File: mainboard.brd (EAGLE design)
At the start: 104.8 x 57.1 mm, 16 parts, among them IC1 7805TV, IC2 7805TV, IC3 7805TV, X1 22-23-2021

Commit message: Add files via upload
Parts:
- removed PERIFERAL: (no value), con-lstb:MA04-1
- removed R3: 120, rcl:0204/7
- removed U$2: PIN_2X2, DUElib130425:PIN_2X2
- removed V4: ALTIMETER_V4, aero_sensors:ALTIMETER_V4
- added MUX1, MUX2: SN74HC157, QADT:SN74HC157
- added R1: 100k, rcl:0204/7
- added U$4: ALTIMETER_V5, aero_sensors:ALTIMETER_V5
- G1: device aero_sensors:GPS_ADAFRUIT -> QADT:GPS_ADAFRUIT
- OUT: value PIN_3X8 -> PIN_3X9; device aero_sensors:PIN_3X8 -> QADT:PIN_3X9
- R2: value 120 -> 30k
- moved MPU 21.2 mm to (65.8, 23.0), turned to 90 degrees
- moved R2 13.1 mm to (68.1, 16.1), turned to 180 degrees
- moved X1 6.05 mm to (24.3, 6.35)
- moved IC3 4.58 mm to (46.5, 15.2)
- moved IC2 3.57 mm to (38.6, 15.2)
- moved G1 3.45 mm to (46.0, 38.4)
- moved XB1 2.99 mm to (82.2, 38.5)
- moved OUT 1.91 mm to (13.1, 17.7)
- moved U$1 1.80 mm to (78.2, 23.1)
- moved U$3 1.80 mm to (8.13, 5.08)
- moved IC1 1.80 mm to (30.2, 15.2)
- moved REC 1.27 mm to (14.0, 49.0)
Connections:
- removed net FLAP_MODE: REC.3.5, U$1.11
- removed net LED_ON: PERIFERAL.4, R3.1
- removed net LED_TEST: R2.2, U$1.50
- removed net LED_TEST_OUT: PERIFERAL.3, R2.1
- removed net LEFT_TAIL: OUT.3.7, U$1.3
- removed net N$1: U$1.GND_1
- removed net N$3: U$2.1.1, XB1.3
- removed net N$4: U$2.1.2, XB1.2
- removed net PID_MODE: REC.3.6, U$1.7
- removed net PITCH_R: REC.3.3, U$1.8
- removed net RIGHT_TAIL: OUT.3.5, U$1.4
- removed net ROLL_R: REC.3.2, U$1.9
- removed net RUDDER: OUT.3.8, U$1.2
- removed net RX1: G1.RX, U$1.RX1
- removed net SPARE: OUT.3.1, U$1.13
- removed net TX1: G1.TX, U$1.TX1
- removed net YAW_R: REC.3.4, U$1.12
- new net BATTERY_VOLTAGE_IN: R1.1, R2.2, U$1.A4
- new net DUE-TO-GPS: G1.RX, U$1.TX1
- new net FLAPS_IN: MUX2.11, MUX2.14, REC.3.6, U$1.50
- new net FLAPS_LEFT: MUX2.12, OUT.3.8
- new net FLAPS_LEFT_AOUT: MUX2.13, U$1.7
- new net FLAPS_RIGHT: MUX2.9, OUT.3.9
- new net FLAPS_RIGHT_AOUT: MUX2.10, U$1.8
- new net GPS-TO-DUE: G1.TX, U$1.RX1
- new net LEFT_AILERON_AOUT: MUX1.3, U$1.5
- new net LEFT_AILERON_IN: MUX1.2, REC.3.2, U$1.9
- new net LEFT_VTAIL: MUX2.4, OUT.3.4
- new net LEFT_VTAIL_AOUT: MUX2.3, U$1.3
- new net LEFT_VTAIL_IN: MUX2.2, REC.3.4, U$1.11
- new net RIGHT_AILERON_AOUT: MUX1.6, U$1.6
- new net RIGHT_AILERON_IN: MUX1.5, REC.3.3, U$1.10
- new net RIGHT_VTAIL: MUX2.7, OUT.3.5
- new net RIGHT_VTAIL_AOUT: MUX2.6, U$1.4
- new net RIGHT_VTAIL_IN: MUX2.5, REC.3.5, U$1.12
- new net TAIL_WHEEL: OUT.3.7, U$1.2
- net +5V: now also MUX1.1, MUX2.1; no longer REC.2.1, REC.2.2, REC.2.3, REC.2.4, REC.2.5, REC.2.6, V4.VIN
- net 12V: now also R1.2
- net 3.3V: now also U$4.VIN; no longer R3.2
- net DROP: now also OUT.3.1, U$1.13; no longer OUT.3.2, U$1.10
- net GND: now also MUX1.15, MUX1.8, MUX2.15, MUX2.8, OUT.1.9, R2.1, U$1.GND_1, U$4.GND; no longer PERIFERAL.1, V4.GND
- net LEFT_AILERON: now also MUX1.4, OUT.3.2; no longer OUT.3.3, U$1.6
- net RESET: no longer PERIFERAL.2
- net RIGHT_AILERON: now also MUX1.7, OUT.3.3; no longer OUT.3.4, U$1.5
- net RX: now also XB1.2; no longer U$2.2.2
- net SCL: now also U$4.SCL; no longer V4.SCL
- net SDA: now also U$4.SDA; no longer V4.SDA
- net SERVO_PWR: now also MUX1.16, MUX2.16, OUT.2.9, REC.2.1, REC.2.2, REC.2.3, REC.2.4, REC.2.5, REC.2.6
- net TX: now also XB1.3; no longer U$2.2.1
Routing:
- net FLAPS_IN: track 0.00 -> 190.6 mm, vias 0 -> 5
- net SERVO_PWR: track 46.6 -> 190.3 mm, vias 0 -> 3
- net LEFT_VTAIL_IN: track 0.00 -> 111.8 mm, vias 0 -> 5
- net +5V: track 154.7 -> 71.1 mm, vias 2 -> 1
- net TX1: track 75.4 -> 0.00 mm, vias 2 -> 0
- net RIGHT_TAIL: track 70.7 -> 0.00 mm
- net LEFT_TAIL: track 69.1 -> 0.00 mm
- net RUDDER: track 69.1 -> 0.00 mm
- net TAIL_WHEEL: track 0.00 -> 68.6 mm
- net RESET: track 65.3 -> 0.00 mm, vias 2 -> 0
- net LEFT_AILERON_IN: track 0.00 -> 63.8 mm, vias 0 -> 1
- net PID_MODE: track 61.7 -> 0.00 mm
- net FLAP_MODE: track 59.9 -> 0.00 mm
- net RIGHT_AILERON_IN: track 0.00 -> 58.3 mm, vias 0 -> 2
- net SPARE: track 57.7 -> 0.00 mm, vias 1 -> 0
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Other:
- board size 104.8 x 57.1 mm -> 103.5 x 57.2 mm
- board text added: "FL"
- board text added: "GND"
- board text added: "LF"
- board text added: "RF"
- board text added: "TW"
- board text removed: "ELV"
- board text removed: "G"
- board text removed: "P"
- board text removed: "PID"
- board text removed: "PROG"
- board text removed: "R"
- board text removed: "RU"
- board text removed: "SP"
- board text removed: "T"

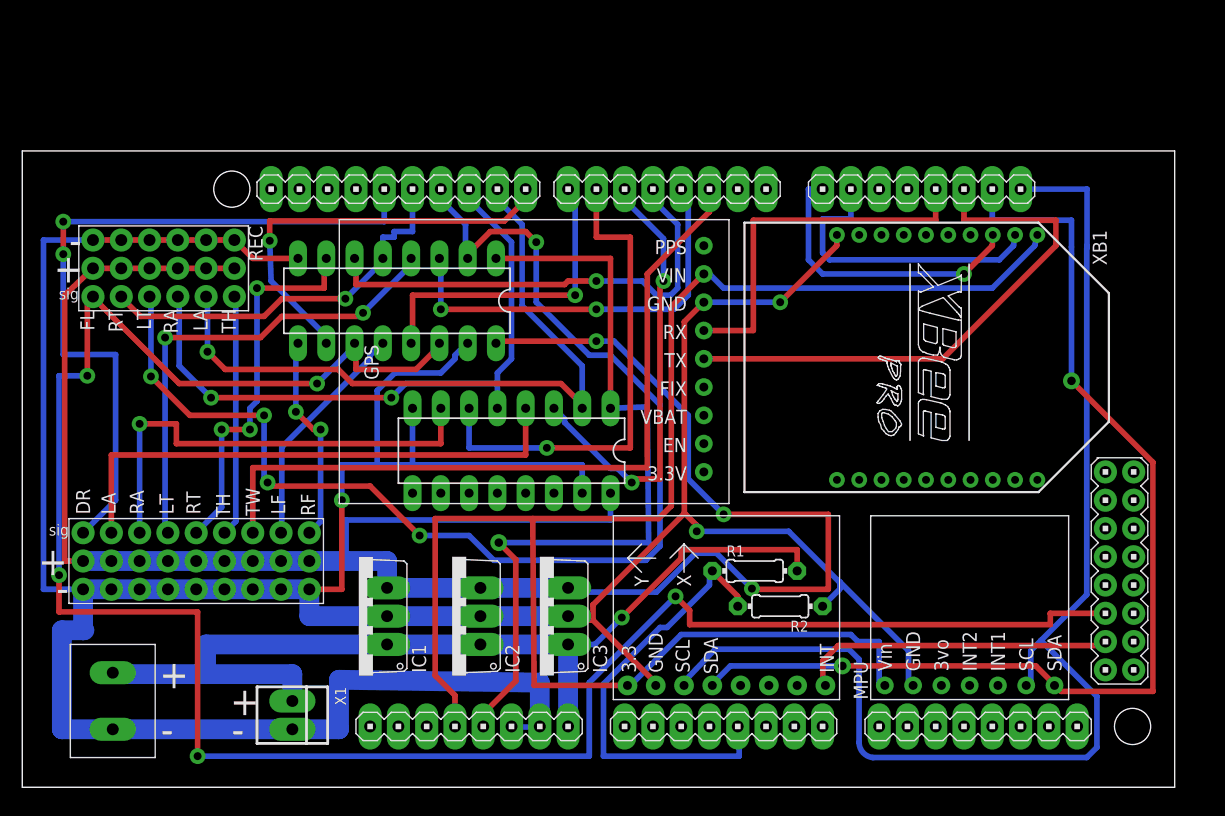
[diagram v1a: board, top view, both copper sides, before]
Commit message: Board with Four Holes
Added top-right and bottom-left hole
Hole placement based on Arduino due eagle file found on Arduino.com
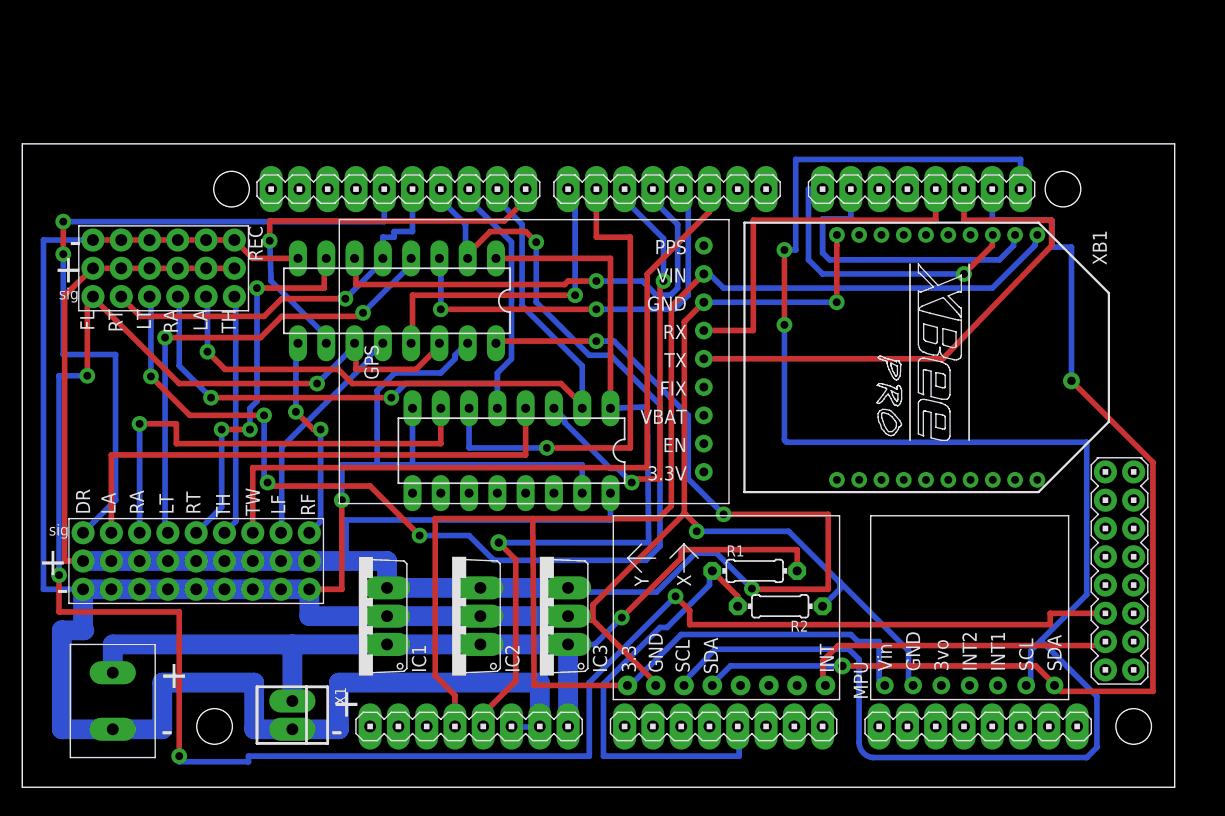
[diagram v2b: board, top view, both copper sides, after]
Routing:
- net SCL: track 111.9 -> 159.5 mm, vias 0 -> 2
- net GND: track 323.4 -> 334.5 mm
- net 12V: track 88.2 -> 83.0 mm
- net FLAPS_IN: track 190.6 -> 191.6 mm
- net GPS-TO-DUE: track 49.2 -> 48.5 mm
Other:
- board size 103.5 x 57.2 mm -> 103.5 x 57.8 mm

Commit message: Add files via upload
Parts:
- OUT: value PIN_3X9 -> PIN_3X10; device QADT:PIN_3X9 -> QADT:PIN_3X10
- moved MUX1 16.6 mm to (34.2, 43.6), turned to 0 degrees
- moved MUX2 16.4 mm to (43.1, 30.1), turned to 0 degrees
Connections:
- new net MUX_SELECT_A: MUX1.1, U$1.44
- new net MUX_SELECT_B: MUX2.1, U$1.46
- new net SPARE: OUT.3.10, U$1.9
- net +5V: no longer MUX1.1, MUX2.1
- net GND: now also OUT.1.10; no longer MUX1.15
- net LEFT_AILERON_IN: now also U$1.40; no longer U$1.9
- net LEFT_VTAIL: now also MUX1.12; no longer MUX2.4
- net LEFT_VTAIL_AOUT: now also MUX1.13; no longer MUX2.3
- net LEFT_VTAIL_IN: now also MUX1.14, MUX1.15; no longer MUX2.2
- net RIGHT_VTAIL: now also MUX1.9; no longer MUX2.7
- net RIGHT_VTAIL_AOUT: now also MUX1.10; no longer MUX2.6
- net RIGHT_VTAIL_IN: now also MUX1.11; no longer MUX2.5
- net SERVO_PWR: now also OUT.2.10
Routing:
- net LEFT_AILERON_IN: track 63.8 -> 188.5 mm, vias 1 -> 5
- net LEFT_VTAIL: track 43.1 -> 147.3 mm, vias 2 -> 3
- net MUX_SELECT_B: track 0.00 -> 102.3 mm, vias 0 -> 6
- net MUX_SELECT_A: track 0.00 -> 90.5 mm, vias 0 -> 6
- net LEFT_VTAIL_IN: track 111.8 -> 33.8 mm, vias 5 -> 0
- net SPARE: track 0.00 -> 74.8 mm, vias 0 -> 3
- net +5V: track 71.1 -> 0.00 mm, vias 1 -> 0
- net GND: track 334.5 -> 302.0 mm
- net FLAPS_RIGHT: track 18.8 -> 50.8 mm, vias 2 -> 1
- net FLAPS_LEFT: track 20.8 -> 50.0 mm, vias 0 -> 1
- net RIGHT_VTAIL_AOUT: track 42.0 -> 19.4 mm
- net 3.3V: track 148.4 -> 131.0 mm
- net SERVO_PWR: track 190.3 -> 173.6 mm
- net FLAPS_RIGHT_AOUT: track 37.8 -> 25.1 mm
- net RIGHT_AILERON_AOUT: track 44.3 -> 32.9 mm, vias 1 -> 2
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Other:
- board size 103.5 x 57.8 mm -> 104.6 x 57.8 mm
- board text added: "SP"

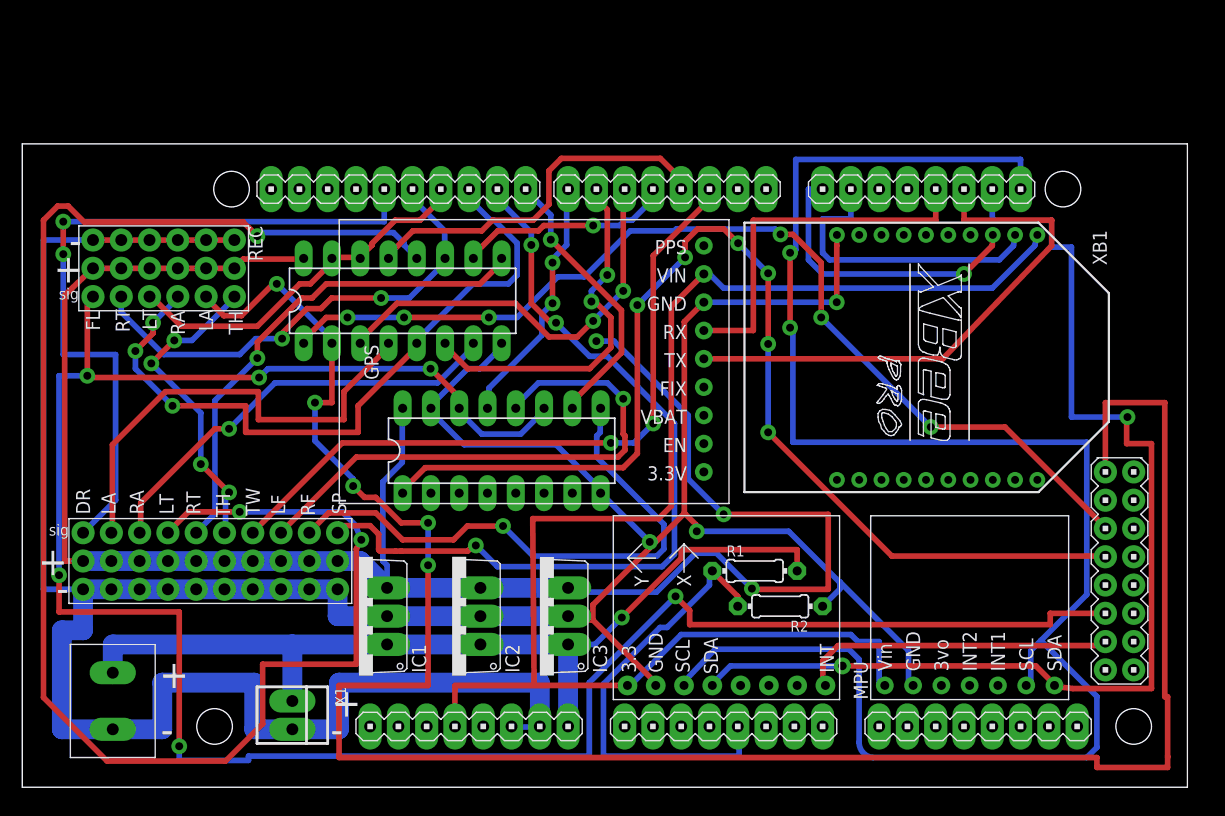
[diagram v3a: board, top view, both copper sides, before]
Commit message: ERC error fixed
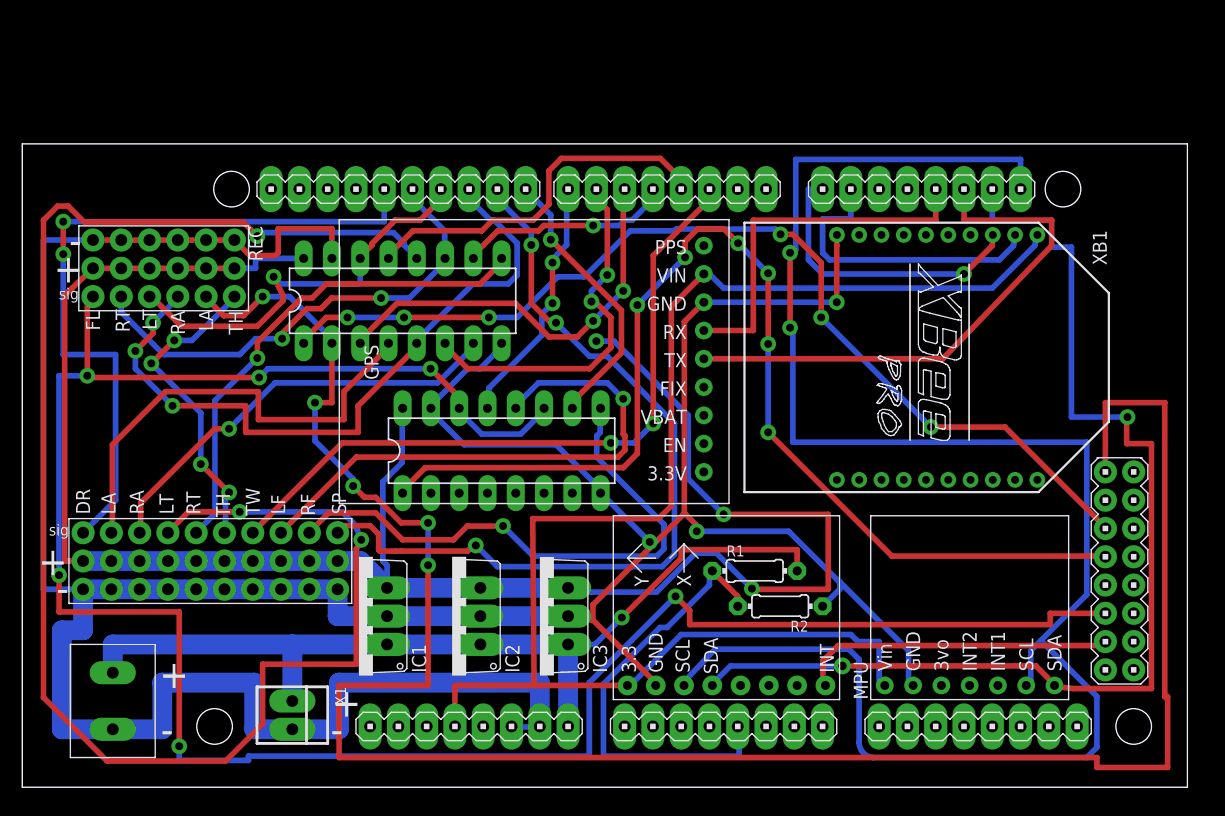
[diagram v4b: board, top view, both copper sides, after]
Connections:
- net GND: now also MUX1.15
- net LEFT_VTAIL_IN: no longer MUX1.15
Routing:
- net GND: track 302.0 -> 316.3 mm
- net LEFT_VTAIL_IN: track 33.8 -> 37.4 mm, vias 0 -> 1
- net LEFT_AILERON_IN: track 188.5 -> 187.6 mm
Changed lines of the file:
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@@
 <wire x1="52.07" y1="26.19375" x2="51.943" y2="26.289" width="0.508" layer="16"/>
 <via x="56.35625" y="21.9075" extent="1-16" drill="0.7112"/>
+<contactref element="MUX1" pad="15"/>
+<wire x1="19.05" y1="49.022" x2="20.447" y2="47.625" width="0.508" layer="1"/>
+<wire x1="20.447" y1="47.625" x2="22.733" y2="47.625" width="0.508" layer="1"/>
+<wire x1="22.733" y1="47.625" x2="22.987" y2="47.879" width="0.508" layer="1"/>
+<wire x1="22.987" y1="47.879" x2="22.987" y2="50.038" width="0.508" layer="1"/>
+<wire x1="22.987" y1="50.038" x2="27.813" y2="50.038" width="0.508" layer="1"/>
+<wire x1="27.813" y1="50.038" x2="27.813" y2="47.371" width="0.508" layer="1"/>
 </signal>
 <signal name="LEFT_AILERON">
@@
 <wire x1="32.385" y1="20.193" x2="32.385" y2="27.305" width="0.508" layer="16"/>
 <wire x1="34.13125" y1="33.81375" x2="34.163" y2="33.909" width="0.508" layer="16"/>
-<wire x1="19.84375" y1="47.3075" x2="25.24125" y2="47.3075" width="0.508" layer="1"/>
-<wire x1="19.20875" y1="46.6725" x2="19.84375" y2="47.3075" width="0.508" layer="1"/>
-<wire x1="25.24125" y1="47.3075" x2="25.273" y2="47.371" width="0.508" layer="1"/>
-<wire x1="19.20875" y1="46.6725" x2="19.05" y2="46.482" width="0.508" layer="1"/>
 <wire x1="32.766" y1="17.78" x2="30.353" y2="20.193" width="1.778" layer="16"/>
 <wire x1="30.353" y1="20.193" x2="28.321" y2="20.193" width="1.778" layer="16"/>
 <wire x1="32.385" y1="20.193" x2="32.766" y2="19.812" width="0.508" layer="16"/>
 <wire x1="32.766" y1="19.812" x2="32.766" y2="17.78" width="0.508" layer="16"/>
+<wire x1="25.273" y1="47.371" x2="20.955" y2="47.371" width="0.508" layer="16"/>
+<wire x1="20.955" y1="47.371" x2="20.955" y2="46.482" width="0.508" layer="16"/>
+<wire x1="20.955" y1="46.482" x2="19.05" y2="46.482" width="0.508" layer="16"/>
 </signal>
 <signal name="12V">
@@
 <contactref element="MUX1" pad="2"/>
 <wire x1="27.78125" y1="40.16375" x2="27.78125" y2="39.84625" width="0.508" layer="16"/>
-<wire x1="22.86" y1="45.085" x2="27.78125" y2="40.16375" width="0.508" layer="16"/>
-<wire x1="22.5425" y1="45.085" x2="22.86" y2="45.085" width="0.508" layer="1"/>
-<wire x1="19.685" y1="42.2275" x2="22.5425" y2="45.085" width="0.508" layer="1"/>
-<wire x1="18.0975" y1="42.2275" x2="19.685" y2="42.2275" width="0.508" layer="1"/>
+<wire x1="18.0975" y1="42.2275" x2="19.8755" y2="42.2275" width="0.508" layer="1"/>
 <wire x1="16.51" y1="43.815" x2="18.0975" y2="42.2275" width="0.508" layer="1"/>
 <wire x1="27.78125" y1="39.84625" x2="27.813" y2="39.751" width="0.508" layer="16"/>
 <wire x1="16.51" y1="43.815" x2="16.51" y2="43.942" width="0.508" layer="1"/>
-<via x="22.86" y="45.085" extent="1-16" drill="0.7112"/>
+<via x="21.59" y="43.942" extent="1-16" drill="0.7112"/>
 <contactref element="U$1" pad="40"/>
 <wire x1="97.282" y1="28.194" x2="97.282" y2="34.417" width="0.508" layer="1"/>
@@
 <wire x1="102.616" y1="34.417" x2="102.616" y2="8.001" width="0.508" layer="1"/>
 <wire x1="102.616" y1="8.001" x2="102.87" y2="8.001" width="0.508" layer="1"/>
-<wire x1="102.87" y1="8.001" x2="102.87" y2="2.667" width="0.508" layer="1"/>
-<wire x1="102.87" y1="2.667" x2="102.87" y2="2.54" width="0.508" layer="1"/>
+<wire x1="102.87" y1="8.001" x2="102.87" y2="1.651" width="0.508" layer="1"/>
 <wire x1="28.448" y1="2.54" x2="96.52" y2="2.54" width="0.508" layer="1"/>
 <wire x1="96.52" y1="2.54" x2="96.52" y2="1.651" width="0.508" layer="1"/>
 <wire x1="96.52" y1="1.651" x2="102.87" y2="1.651" width="0.508" layer="1"/>
-<wire x1="102.87" y1="1.651" x2="102.87" y2="2.54" width="0.508" layer="1"/>
+<wire x1="27.78125" y1="40.16375" x2="24.003" y2="43.942" width="0.508" layer="16"/>
+<wire x1="24.003" y1="43.942" x2="21.59" y2="43.942" width="0.508" layer="16"/>
+<wire x1="21.59" y1="43.942" x2="19.8755" y2="42.2275" width="0.508" layer="1"/>
 </signal>
 <signal name="RIGHT_AILERON_IN">
@@
 <contactref element="REC" pad="3.4"/>
 <contactref element="U$1" pad="11"/>
-<contactref element="MUX1" pad="15"/>
 <contactref element="MUX1" pad="14"/>
-<wire x1="30.32125" y1="47.46625" x2="27.94" y2="47.46625" width="0.508" layer="1"/>
-<wire x1="27.94" y1="47.46625" x2="27.813" y2="47.371" width="0.508" layer="1"/>
 <wire x1="30.32125" y1="47.46625" x2="30.353" y2="47.371" width="0.508" layer="1"/>
 <wire x1="31.4325" y1="48.5775" x2="30.48" y2="47.625" width="0.508" layer="1"/>
@@
 <wire x1="14.2875" y1="41.275" x2="11.7475" y2="43.815" width="0.508" layer="1"/>
 <wire x1="21.11375" y1="41.275" x2="14.2875" y2="41.275" width="0.508" layer="1"/>
-<wire x1="24.92375" y1="45.085" x2="21.11375" y2="41.275" width="0.508" layer="1"/>
-<wire x1="25.87625" y1="45.085" x2="24.92375" y2="45.085" width="0.508" layer="1"/>
-<wire x1="28.09875" y1="47.3075" x2="25.87625" y2="45.085" width="0.508" layer="1"/>
+<wire x1="22.57425" y1="45.72" x2="23.39975" y2="44.069" width="0.508" layer="1"/>
 <wire x1="11.43" y1="43.815" x2="11.43" y2="43.942" width="0.508" layer="1"/>
-<wire x1="28.09875" y1="47.3075" x2="27.813" y2="47.371" width="0.508" layer="1"/>
+<via x="22.57425" y="45.72" extent="1-16" drill="0.7112"/>
+<wire x1="30.353" y1="45.085" x2="30.353" y2="47.371" width="0.508" layer="16"/>
+<wire x1="22.57425" y1="45.72" x2="23.20925" y2="45.085" width="0.508" layer="16"/>
+<wire x1="23.20925" y1="45.085" x2="30.353" y2="45.085" width="0.508" layer="16"/>
+<wire x1="23.39975" y1="43.561" x2="21.11375" y2="41.275" width="0.508" layer="1"/>
+<wire x1="23.39975" y1="44.069" x2="23.39975" y2="43.561" width="0.508" layer="1"/>
 </signal>
 <signal name="RIGHT_VTAIL_IN">
